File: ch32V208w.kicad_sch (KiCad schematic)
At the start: 25 parts, among them J1 TC2050, J2 DNP, J3 DNP, U1 CH32V208WBU6, Y1 32MHz, Y2 32768Hz

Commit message: Changed outline for DFM
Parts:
- C1, C11, C2, C3, C4, C5, C6, C7: JLCPCB Part # C359190 -> (none); LCSC (none) -> C359190
- C10: JLCPCB Part # C307340 -> (none); LCSC (none) -> C307340
- C12, C13: JLCPCB Part # C472446 -> (none); LCSC (none) -> C472446
- C14, C15: JLCPCB Part # C86285 -> (none); LCSC (none) -> C86285
- C8: JLCPCB Part # C315248 -> (none); LCSC (none) -> C315248
- C9: JLCPCB Part # C170150 -> (none); LCSC (none) -> C170150
- L1: JLCPCB Part # C87530 -> (none); LCSC (none) -> C87530
- R1, R2: JLCPCB Part # C2906885 -> (none); LCSC (none) -> C2906885
- U1: JLCPCB Part # C5187528 -> (none); LCSC (none) -> C5187528
- Y1: JLCPCB Part # C9009 -> (none); LCSC (none) -> C9009
- Y2: JLCPCB Part # C725996 -> (none); LCSC (none) -> C725996
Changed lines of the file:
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@@
       (effects (font (size 1.27 1.27)) hide)
     )
-    (property "JLCPCB Part #" "C2906885" (at 220.98 138.43 0)
+    (property "LCSC" "C2906885" (at 220.98 138.43 0)
       (effects (font (size 1.27 1.27)) hide)
     )
@@
       (effects (font (size 1.27 1.27)) hide)
     )
-    (property "JLCPCB Part #" "C9009" (at 34.29 88.9 0)
+    (property "LCSC" "C9009" (at 34.29 88.9 0)
       (effects (font (size 1.27 1.27)) hide)
     )
@@
       (effects (font (size 1.27 1.27)) hide)
     )
-    (property "JLCPCB Part #" "C359190" (at 140.97 143.51 0)
+    (property "LCSC" "C359190" (at 140.97 143.51 0)
       (effects (font (size 1.27 1.27)) hide)
     )
@@
       (effects (font (size 1.27 1.27)) hide)
     )
-    (property "JLCPCB Part #" "C359190" (at 118.11 44.45 0)
+    (property "LCSC" "C359190" (at 118.11 44.45 0)
       (effects (font (size 1.27 1.27)) hide)
     )
@@
       (effects (font (size 1.27 1.27)) hide)
     )
-    (property "JLCPCB Part #" "C359190" (at 78.74 102.87 0)
+    (property "LCSC" "C359190" (at 78.74 102.87 0)
       (effects (font (size 1.27 1.27)) hide)
     )
@@
       (effects (font (size 1.27 1.27)) hide)
     )
-    (property "JLCPCB Part #" "C86285" (at 30.48 110.49 0)
+    (property "LCSC" "C86285" (at 30.48 110.49 0)
       (effects (font (size 1.27 1.27)) hide)
     )
@@
       (effects (font (size 1.27 1.27)) hide)
     )
-    (property "JLCPCB Part #" "C359190" (at 151.13 143.51 0)
+    (property "LCSC" "C359190" (at 151.13 143.51 0)
       (effects (font (size 1.27 1.27)) hide)
     )
@@
       (effects (font (size 1.27 1.27)) hide)
     )
-    (property "JLCPCB Part #" "C307340" (at 191.77 62.23 0)
+    (property "LCSC" "C307340" (at 191.77 62.23 0)
       (effects (font (size 1.27 1.27)) hide)
     )
@@
       (effects (font (size 1.27 1.27)) hide)
     )
-    (property "JLCPCB Part #" "C359190" (at 78.74 120.65 0)
+    (property "LCSC" "C359190" (at 78.74 120.65 0)
       (effects (font (size 1.27 1.27)) hide)
     )
@@
       (effects (font (size 1.27 1.27)) hide)
     )
-    (property "JLCPCB Part #" "C472446" (at 30.48 81.28 0)
+    (property "LCSC" "C472446" (at 30.48 81.28 0)
       (effects (font (size 1.27 1.27)) hide)
     )
@@
       (effects (font (size 1.27 1.27)) hide)
     )
-    (property "JLCPCB Part #" "C725996" (at 34.29 118.11 0)
+    (property "LCSC" "C725996" (at 34.29 118.11 0)
       (effects (font (size 1.27 1.27)) hide)
     )
@@
       (effects (font (size 1.27 1.27)) hide)
     )
-    (property "JLCPCB Part #" "" (at 187.96 35.56 0)
+    (property "LCSC" "" (at 187.96 35.56 0)
       (effects (font (size 1.27 1.27)) hide)
     )
@@
       (effects (font (size 1.27 1.27)) hide)
     )
-    (property "JLCPCB Part #" "C359190" (at 80.01 76.2 0)
+    (property "LCSC" "C359190" (at 80.01 76.2 0)
       (effects (font (size 1.27 1.27)) hide)
     )
@@
       (effects (font (size 1.27 1.27)) hide)
     )
-    (property "JLCPCB Part #" "C2906885" (at 137.16 135.89 0)
+    (property "LCSC" "C2906885" (at 137.16 135.89 0)
       (effects (font (size 1.27 1.27)) hide)
     )
@@
       (effects (font (size 1.27 1.27)) hide)
     )
-    (property "JLCPCB Part #" "C472446" (at 30.48 96.52 0)
+    (property "LCSC" "C472446" (at 30.48 96.52 0)
       (effects (font (size 1.27 1.27)) hide)
     )
@@
       (effects (font (size 1.27 1.27)) hide)
     )
-    (property "JLCPCB Part #" "C86285" (at 30.48 125.73 0)
+    (property "LCSC" "C86285" (at 30.48 125.73 0)
       (effects (font (size 1.27 1.27)) hide)
     )
@@
       (effects (font (size 1.27 1.27)) hide)
     )
-    (property "JLCPCB Part #" "" (at 227.33 144.78 0)
+    (property "LCSC" "" (at 227.33 144.78 0)
       (effects (font (size 1.27 1.27)) hide)
     )
@@
       (effects (font (size 1.27 1.27)) hide)
     )
-    (property "JLCPCB Part #" "C359190" (at 81.28 93.98 0)
+    (property "LCSC" "C359190" (at 81.28 93.98 0)
       (effects (font (size 1.27 1.27)) hide)
     )
@@
       (effects (font (size 1.27 1.27)) hide)
     )
-    (property "JLCPCB Part #" "C359190" (at 107.95 44.45 0)
+    (property "LCSC" "C359190" (at 107.95 44.45 0)
       (effects (font (size 1.27 1.27)) hide)
     )
@@
       (effects (font (size 1.27 1.27)) hide)
     )
-    (property "JLCPCB Part #" "" (at 227.33 93.98 0)
+    (property "LCSC" "" (at 227.33 93.98 0)
       (effects (font (size 1.27 1.27)) hide)
     )
@@
       (effects (font (size 1.27 1.27)) hide)
     )
-    (property "JLCPCB Part #" "" (at 227.33 106.68 0)
+    (property "LCSC" "" (at 227.33 106.68 0)
       (effects (font (size 1.27 1.27)) hide)
     )
@@
       (effects (font (size 1.27 1.27)) hide)
     )
-    (property "JLCPCB Part #" "C87530" (at 187.96 57.15 0)
+    (property "LCSC" "C87530" (at 187.96 57.15 0)
       (effects (font (size 1.27 1.27)) hide)
     )
@@
       (effects (font (size 1.27 1.27)) hide)
     )
-    (property "JLCPCB Part #" "C170150" (at 191.77 50.8 0)
+    (property "LCSC" "C170150" (at 191.77 50.8 0)
       (effects (font (size 1.27 1.27)) hide)
     )
@@
       (effects (font (size 1.27 1.27)) hide)
     )
-    (property "JLCPCB Part #" "C315248" (at 177.8 78.74 0)
+    (property "LCSC" "C315248" (at 177.8 78.74 0)
       (effects (font (size 1.27 1.27)) hide)
     )
@@
       (effects (font (size 1.27 1.27)) hide)
     )
-    (property "JLCPCB Part #" "C5187528" (at 132.08 93.98 0)
-      (effects (font (size 1.27 1.27)) hide)
-    )
+    (property "LCSC" "C5187528" (at 132.08 93.98 0)
+      (effects (font (size 1.27 1.27)) hide)
+    )

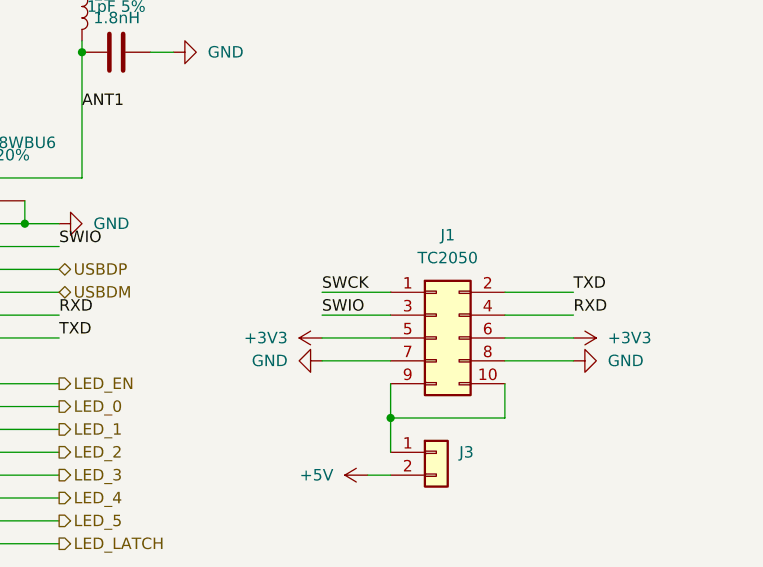
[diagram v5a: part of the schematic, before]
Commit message: Delta for future Debugger interfaces
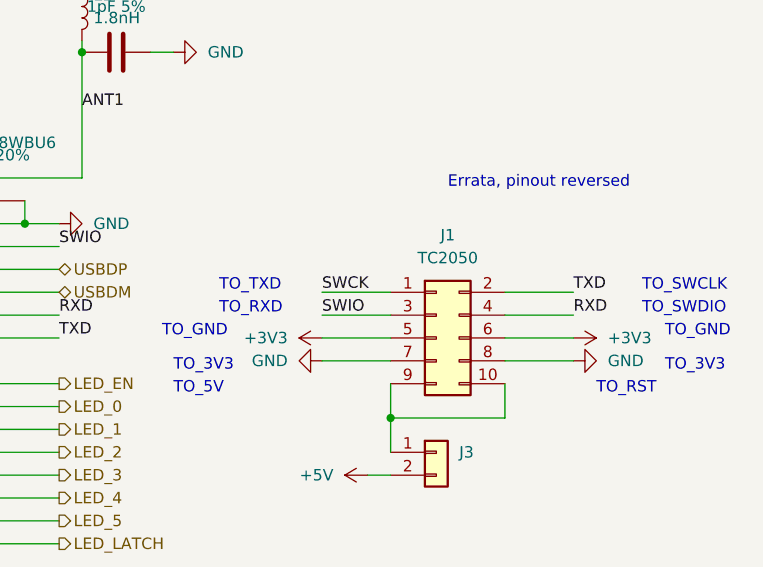
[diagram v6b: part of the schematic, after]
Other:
- note added: "Errata, pinout reversed"
- note added: "TO_3V3"
- note added: "TO_5V"
- note added: "TO_GND"
- note added: "TO_RST"
- note added: "TO_RXD"
- note added: "TO_SWCLK"
- note added: "TO_SWDIO"
- note added: "TO_TXD"
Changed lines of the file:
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@@
     (stroke (width 0) (type default))
+  )
+  (text "TO_GND" (at 252.73 93.98 0)
+    (effects (font (size 1.27 1.27)) (justify left bottom))
+  )
+  (text "Errata, pinout reversed" (at 228.6 77.47 0)
+    (effects (font (size 1.27 1.27)) (justify left bottom))
+  )
+  (text "TO_RXD" (at 203.2 91.44 0)
+    (effects (font (size 1.27 1.27)) (justify left bottom))
+  )
+  (text "TO_5V" (at 198.12 100.33 0)
+    (effects (font (size 1.27 1.27)) (justify left bottom))
+  )
+  (text "TO_RST" (at 245.11 100.33 0)
+    (effects (font (size 1.27 1.27)) (justify left bottom))
+  )
+  (text "TO_SWCLK" (at 250.19 88.9 0)
+    (effects (font (size 1.27 1.27)) (justify left bottom))
+  )
+  (text "TO_3V3" (at 198.12 97.79 0)
+    (effects (font (size 1.27 1.27)) (justify left bottom))
+  )
+  (text "TO_SWDIO" (at 250.19 91.44 0)
+    (effects (font (size 1.27 1.27)) (justify left bottom))
+  )
+  (text "TO_TXD" (at 203.2 88.9 0)
+    (effects (font (size 1.27 1.27)) (justify left bottom))
+  )
+  (text "TO_GND" (at 196.85 93.98 0)
+    (effects (font (size 1.27 1.27)) (justify left bottom))
+  )
+  (text "TO_3V3" (at 252.73 97.79 0)
+    (effects (font (size 1.27 1.27)) (justify left bottom))
   )
   (label "SWCK" (at 214.63 88.9 0) (fields_autoplaced)
